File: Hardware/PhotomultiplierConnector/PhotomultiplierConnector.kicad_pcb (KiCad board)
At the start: 2 copper layers, 0 parts

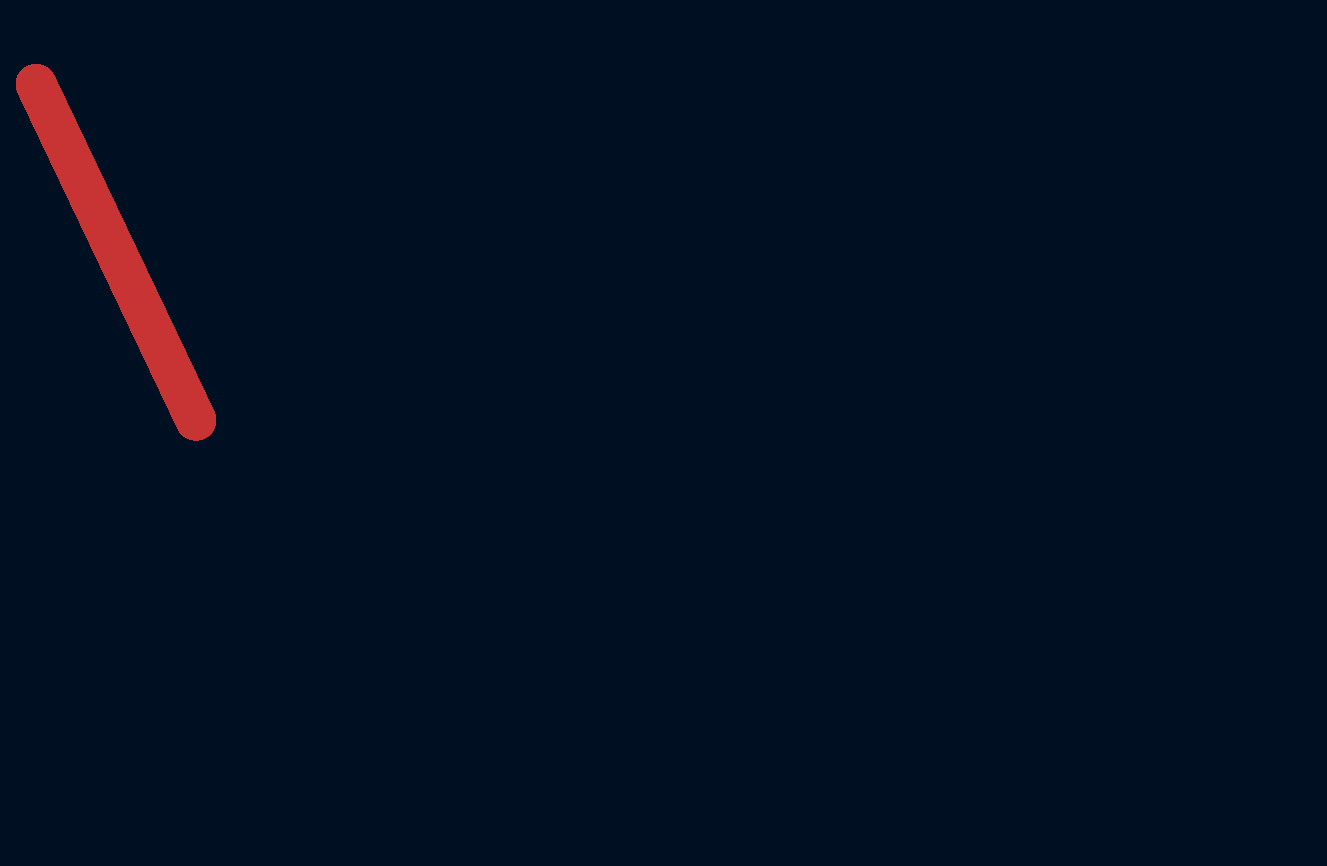
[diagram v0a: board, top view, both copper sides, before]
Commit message: finished script for automatic component placement - it was overengineering, abandonend ide aof a circular pcb for photomultiplier connector
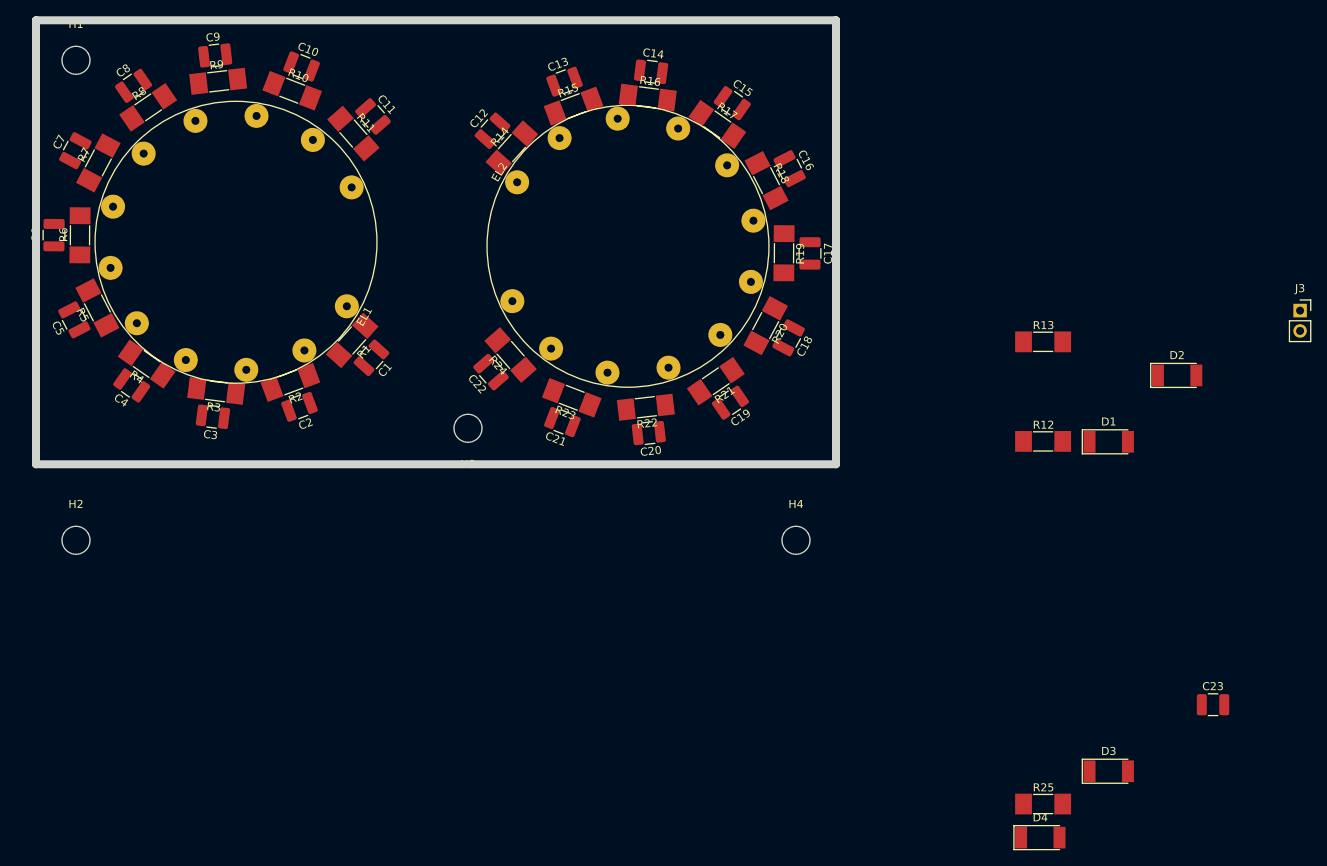
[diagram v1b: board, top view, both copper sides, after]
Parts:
- added C1: 10n/3kV, Capacitor_SMD:C_1210_3225Metric, F.Cu at (41.9, 42.2)
- added C10: 10n/3kV, Capacitor_SMD:C_1210_3225Metric, F.Cu at (33.2, 5.78)
- added C11: 10n/3kV, Capacitor_SMD:C_1210_3225Metric, F.Cu at (42.1, 12.0)
- added C12: 10n/3kV, Capacitor_SMD:C_1210_3225Metric, F.Cu at (57.1, 13.8)
- added C13: 10n/3kV, Capacitor_SMD:C_1210_3225Metric, F.Cu at (66.1, 7.68)
- added C14: 10n/3kV, Capacitor_SMD:C_1210_3225Metric, F.Cu at (76.9, 6.43)
- added C15: 10n/3kV, Capacitor_SMD:C_1210_3225Metric, F.Cu at (87.0, 10.4)
- added C16: 10n/3kV, Capacitor_SMD:C_1210_3225Metric, F.Cu at (94.2, 18.6)
- added C17: 10n/3kV, Capacitor_SMD:C_1210_3225Metric, F.Cu at (96.7, 29.1)
- added C18: 10n/3kV, Capacitor_SMD:C_1210_3225Metric, F.Cu at (94.1, 39.7)
- added C19: 10n/3kV, Capacitor_SMD:C_1210_3225Metric, F.Cu at (86.8, 47.8)
- added C2: 10n/3kV, Capacitor_SMD:C_1210_3225Metric, F.Cu at (32.9, 48.3)
- added C20: 10n/3kV, Capacitor_SMD:C_1210_3225Metric, F.Cu at (76.6, 51.6)
- added C21: 10n/3kV, Capacitor_SMD:C_1210_3225Metric, F.Cu at (65.8, 50.2)
- added C22: 10n/3kV, Capacitor_SMD:C_1210_3225Metric, F.Cu at (56.9, 44.0)
- added C23: 10n/3kV, Capacitor_SMD:C_1210_3225Metric, F.Cu at (147.1, 85.6)
- added C3: 10n/3kV, Capacitor_SMD:C_1210_3225Metric, F.Cu at (22.1, 49.6)
- added C4: 10n/3kV, Capacitor_SMD:C_1210_3225Metric, F.Cu at (12.0, 45.6)
- added C5: 10n/3kV, Capacitor_SMD:C_1210_3225Metric, F.Cu at (4.79, 37.4)
- added C6: 10n/3kV, Capacitor_SMD:C_1210_3225Metric, F.Cu at (2.25, 26.9)
- added C7: 10n/3kV, Capacitor_SMD:C_1210_3225Metric, F.Cu at (4.92, 16.3)
- added C8: 10n/3kV, Capacitor_SMD:C_1210_3225Metric, F.Cu at (12.2, 8.20)
- added C9: 10n/3kV, Capacitor_SMD:C_1210_3225Metric, F.Cu at (22.4, 4.40)
- added D1: 1n148, Diode_SMD:D_MELF, F.Cu at (134.1, 52.7)
- added D2: 1n148, Diode_SMD:D_MELF, F.Cu at (142.6, 44.4)
- added D3: 1n148, Diode_SMD:D_MELF, F.Cu at (134.1, 93.9)
- added D4: 1n148, Diode_SMD:D_MELF, F.Cu at (125.5, 102.2)
- added EL1: Photomultiplier, PhotomultiplierConnector:PhotomultiplierGeneric, F.Cu at (25.0, 27.8)
- added EL2: Photomultiplier, PhotomultiplierConnector:PhotomultiplierGeneric, F.Cu at (74.0, 28.2)
- added H1: MountingHole, MountingHole:MountingHole_3.5mm, F.Cu at (5.00, 5.00)
- added H2: MountingHole, MountingHole:MountingHole_3.5mm, F.Cu at (5.00, 65.0)
- added H3: MountingHole, MountingHole:MountingHole_3.5mm, F.Cu at (54.0, 51.0)
- added H4: MountingHole, MountingHole:MountingHole_3.5mm, F.Cu at (95.0, 65.0)
- added J3: Conn_01x02_Female, Connector_PinSocket_2.54mm:PinSocket_1x02_P2.54mm_Vertical, F.Cu at (158.0, 36.3)
- added R1: 1M, Resistor_SMD:R_MELF_MMB-0207, F.Cu at (39.5, 40.0)
- added R10: 1M, Resistor_SMD:R_MELF_MMB-0207, F.Cu at (32.0, 8.81)
- added R11: 1M, Resistor_SMD:R_MELF_MMB-0207, F.Cu at (39.7, 14.2)
- added R12: 1M, Resistor_SMD:R_MELF_MMB-0207, F.Cu at (125.9, 52.6)
- added R13: 150k, Resistor_SMD:R_MELF_MMB-0207, F.Cu at (125.9, 40.2)
- added R14: 1M, Resistor_SMD:R_MELF_MMB-0207, F.Cu at (59.5, 16.0)
- added R15: 1M, Resistor_SMD:R_MELF_MMB-0207, F.Cu at (67.2, 10.7)
- added R16: 1M, Resistor_SMD:R_MELF_MMB-0207, F.Cu at (76.5, 9.66)
- added R17: 1M, Resistor_SMD:R_MELF_MMB-0207, F.Cu at (85.2, 13.0)
- added R18: 1M, Resistor_SMD:R_MELF_MMB-0207, F.Cu at (91.3, 20.0)
- added R19: 1M, Resistor_SMD:R_MELF_MMB-0207, F.Cu at (93.5, 29.1)
- added R2: 1M, Resistor_SMD:R_MELF_MMB-0207, F.Cu at (31.8, 45.3)
- added R20: 150k, Resistor_SMD:R_MELF_MMB-0207, F.Cu at (91.2, 38.2)
- added R21: 1M, Resistor_SMD:R_MELF_MMB-0207, F.Cu at (85.0, 45.1)
- added R22: 1M, Resistor_SMD:R_MELF_MMB-0207, F.Cu at (76.2, 48.4)
- added R23: 1M, Resistor_SMD:R_MELF_MMB-0207, F.Cu at (67.0, 47.2)
- added R24: 1M, Resistor_SMD:R_MELF_MMB-0207, F.Cu at (59.3, 41.8)
- added R25: 150k, Resistor_SMD:R_MELF_MMB-0207, F.Cu at (125.9, 98.0)
- added R3: 1M, Resistor_SMD:R_MELF_MMB-0207, F.Cu at (22.5, 46.3)
- added R4: 1M, Resistor_SMD:R_MELF_MMB-0207, F.Cu at (13.8, 43.0)
- added R5: 1M, Resistor_SMD:R_MELF_MMB-0207, F.Cu at (7.68, 36.0)
- added R6: 1M, Resistor_SMD:R_MELF_MMB-0207, F.Cu at (5.50, 26.9)
- added R7: 150k, Resistor_SMD:R_MELF_MMB-0207, F.Cu at (7.79, 17.8)
- added R8: 1M, Resistor_SMD:R_MELF_MMB-0207, F.Cu at (14.0, 10.9)
- added R9: 1M, Resistor_SMD:R_MELF_MMB-0207, F.Cu at (22.8, 7.63)
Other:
- board outline added: 100 x 55.5 mm
